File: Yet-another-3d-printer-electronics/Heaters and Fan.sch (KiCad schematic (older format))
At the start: 67 parts, among them P15 HEATER_BED, P16 HEATER_EXT, P18 FAN, P22 FAN, P23 HEATER_EXT, P4 FAN, Q1 2N7000, Q2 IRLR8743PBF, Q3 IRLML0030TRPBF, Q4 IRLR8743PBF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

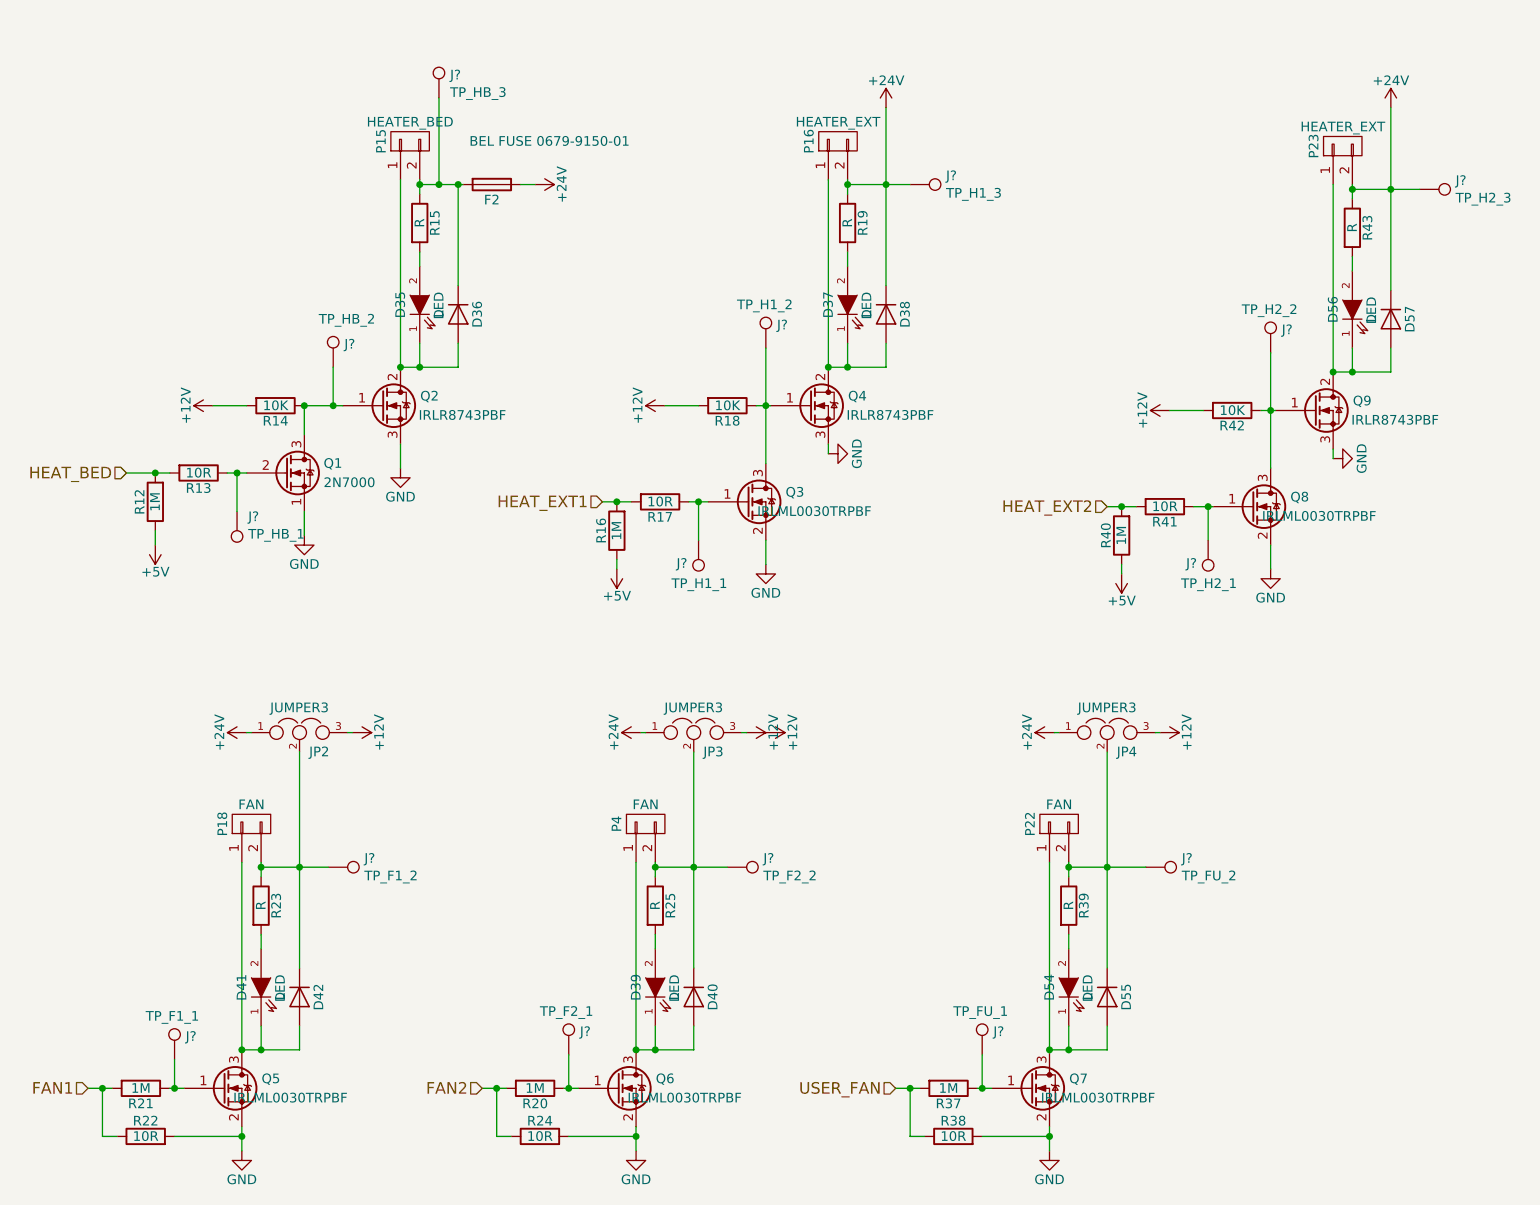
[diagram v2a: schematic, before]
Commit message: Choose footprints for TVS diode, heatbed, heaters, power socket and testpoints
Signed-off-by: Mateusz Krawczuk <mat.krawczuk@gmail.com>
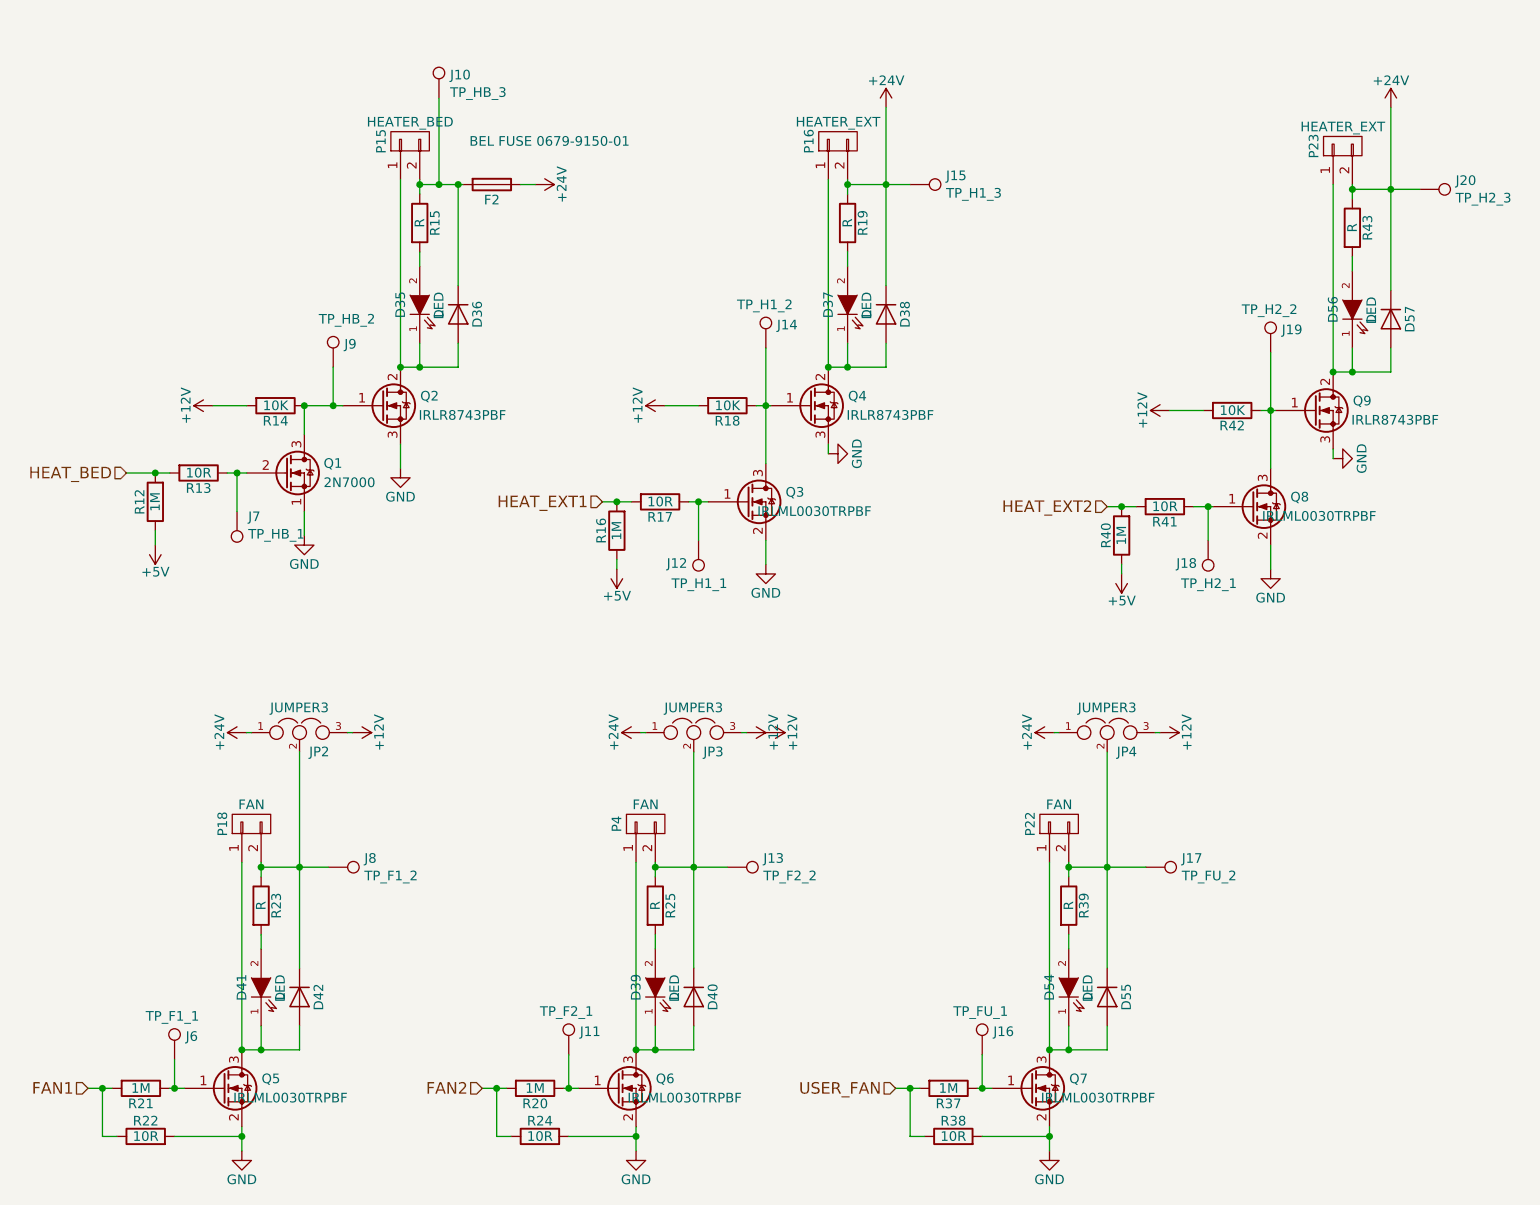
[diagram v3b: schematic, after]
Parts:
- J10, J11, J12, J13, J14, J15, J16, J17, J18, J19, J20, J6, J7, J8, J9: renamed from J?; footprint (none) -> Connect:PINTST
- JP2, JP3, JP4: footprint (none) -> Pin_Headers:Pin_Header_Straight_1x03_Pitch2.54mm
- P15: footprint Connectors:AK300-2 -> Yet-another-3d-printer-electronics:DG300-5.0-02P-12-00A(H)
- P16, P23: footprint Connectors:AK300-2 -> Yet-another-3d-printer-electronics:EBBA-02-C-SS-BU
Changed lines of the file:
@@
 F 0 "P15" H 2550 1775 50  0000 C CNN
 F 1 "HEATER_BED" V 2650 1625 50  0000 C CNN
-F 2 "Connectors:AK300-2" H 2550 1625 50  0001 C CNN
+F 2 "Yet-another-3d-printer-electronics:DG300-5.0-02P-12-00A(H)" H 2550 1625 50  0001 C CNN
 F 3 "" H 2550 1625 50  0000 C CNN
 	1    2550 1625
@@
 F 0 "P16" H 4775 1775 50  0000 C CNN
 F 1 "HEATER_EXT" V 4875 1625 50  0000 C CNN
-F 2 "Connectors:AK300-2" H 4775 1625 50  0001 C CNN
+F 2 "Yet-another-3d-printer-electronics:EBBA-02-C-SS-BU" H 4775 1625 50  0001 C CNN
 F 3 "" H 4775 1625 50  0000 C CNN
 	1    4775 1625
@@
 F 0 "JP2" H 2025 4600 50  0000 L CNN
 F 1 "JUMPER3" H 1975 4800 50  0000 C BNN
-F 2 "" H 1975 4700 50  0001 C CNN
+F 2 "Pin_Headers:Pin_Header_Straight_1x03_Pitch2.54mm" H 1975 4700 50  0001 C CNN
 F 3 "" H 1975 4700 50  0000 C CNN
 	1    1975 4700
@@
 F 0 "JP3" H 4075 4600 50  0000 L CNN
 F 1 "JUMPER3" H 4025 4800 50  0000 C BNN
-F 2 "" H 4025 4700 50  0001 C CNN
+F 2 "Pin_Headers:Pin_Header_Straight_1x03_Pitch2.54mm" H 4025 4700 50  0001 C CNN
 F 3 "" H 4025 4700 50  0000 C CNN
 	1    4025 4700
@@
 F 0 "JP4" H 6225 4600 50  0000 L CNN
 F 1 "JUMPER3" H 6175 4800 50  0000 C BNN
-F 2 "" H 6175 4700 50  0001 C CNN
+F 2 "Pin_Headers:Pin_Header_Straight_1x03_Pitch2.54mm" H 6175 4700 50  0001 C CNN
 F 3 "" H 6175 4700 50  0000 C CNN
 	1    6175 4700
@@
 F 0 "P23" H 7400 1800 50  0000 C CNN
 F 1 "HEATER_EXT" V 7500 1650 50  0000 C CNN
-F 2 "Connectors:AK300-2" H 7400 1650 50  0001 C CNN
+F 2 "Yet-another-3d-printer-electronics:EBBA-02-C-SS-BU" H 7400 1650 50  0001 C CNN
 F 3 "" H 7400 1650 50  0000 C CNN
 	1    7400 1650
@@
 $EndComp
 $Comp
-L TEST_1P J?
+L TEST_1P J10
 U 1 1 5985D991
 P 2700 1400
-F 0 "J?" H 2758 1520 50  0000 L CNN
+F 0 "J10" H 2758 1520 50  0000 L CNN
 F 1 "TP_HB_3" H 2758 1429 50  0000 L CNN
-F 2 "" H 2900 1400 50  0001 C CNN
+F 2 "Connect:PINTST" H 2900 1400 50  0001 C CNN
 F 3 "" H 2900 1400 50  0001 C CNN
 	1    2700 1400
@@
 $EndComp
 $Comp
-L TEST_1P J?
+L TEST_1P J15
 U 1 1 5985EA00
 P 5150 1850
-F 0 "J?" V 5104 2037 50  0000 L CNN
+F 0 "J15" V 5104 2037 50  0000 L CNN
 F 1 "TP_H1_3" V 5195 2037 50  0000 L CNN
-F 2 "" H 5350 1850 50  0001 C CNN
+F 2 "Connect:PINTST" H 5350 1850 50  0001 C CNN
 F 3 "" H 5350 1850 50  0001 C CNN
 	1    5150 1850
@@
 Connection ~ 2700 1850
 $Comp
-L TEST_1P J?
+L TEST_1P J20
 U 1 1 5985F8B9
 P 7800 1875
-F 0 "J?" V 7754 2062 50  0000 L CNN
+F 0 "J20" V 7754 2062 50  0000 L CNN
 F 1 "TP_H2_3" V 7845 2062 50  0000 L CNN
-F 2 "" H 8000 1875 50  0001 C CNN
+F 2 "Connect:PINTST" H 8000 1875 50  0001 C CNN
 F 3 "" H 8000 1875 50  0001 C CNN
 	1    7800 1875
@@
 $EndComp
 $Comp
-L TEST_1P J?
+L TEST_1P J8
 U 1 1 59860366
 P 2125 5400
-F 0 "J?" V 2079 5587 50  0000 L CNN
+F 0 "J8" V 2079 5587 50  0000 L CNN
 F 1 "TP_F1_2" V 2170 5587 50  0000 L CNN
-F 2 "" H 2325 5400 50  0001 C CNN
+F 2 "Connect:PINTST" H 2325 5400 50  0001 C CNN
 F 3 "" H 2325 5400 50  0001 C CNN
 	1    2125 5400
@@
 $EndComp
 $Comp
-L TEST_1P J?
+L TEST_1P J13
 U 1 1 598618D3
 P 4200 5400
-F 0 "J?" V 4154 5587 50  0000 L CNN
+F 0 "J13" V 4154 5587 50  0000 L CNN
 F 1 "TP_F2_2" V 4245 5587 50  0000 L CNN
-F 2 "" H 4400 5400 50  0001 C CNN
+F 2 "Connect:PINTST" H 4400 5400 50  0001 C CNN
 F 3 "" H 4400 5400 50  0001 C CNN
 	1    4200 5400
@@
 $EndComp
 $Comp
-L TEST_1P J?
+L TEST_1P J17
 U 1 1 59861B4C
 P 6375 5400
-F 0 "J?" V 6329 5588 50  0000 L CNN
+F 0 "J17" V 6329 5588 50  0000 L CNN
 F 1 "TP_FU_2" V 6420 5588 50  0000 L CNN
-F 2 "" H 6575 5400 50  0001 C CNN
+F 2 "Connect:PINTST" H 6575 5400 50  0001 C CNN
 F 3 "" H 6575 5400 50  0001 C CNN
 	1    6375 5400
@@
 $EndComp
 $Comp
-L TEST_1P J?
+L TEST_1P J9
 U 1 1 59864703
 P 2150 2800
-F 0 "J?" H 2208 2920 50  0000 L CNN
+F 0 "J9" H 2208 2920 50  0000 L CNN
 F 1 "TP_HB_2" H 2075 3050 50  0000 L CNN
-F 2 "" H 2350 2800 50  0001 C CNN
+F 2 "Connect:PINTST" H 2350 2800 50  0001 C CNN
 F 3 "" H 2350 2800 50  0001 C CNN
 	1    2150 2800
@@
 $EndComp
 $Comp
-L TEST_1P J?
+L TEST_1P J7
 U 1 1 59864CF5
 P 1650 3550
-F 0 "J?" H 1592 3577 50  0000 R CNN
+F 0 "J7" H 1592 3577 50  0000 R CNN
 F 1 "TP_HB_1" H 1592 3668 50  0000 R CNN
-F 2 "" H 1850 3550 50  0001 C CNN
+F 2 "Connect:PINTST" H 1850 3550 50  0001 C CNN
 F 3 "" H 1850 3550 50  0001 C CNN
 	1    1650 3550
@@
 Connection ~ 2150 3000
 $Comp
-L TEST_1P J?
+L TEST_1P J14
 U 1 1 59865BF7
 P 4400 2700
-F 0 "J?" H 4458 2820 50  0000 L CNN
+F 0 "J14" H 4458 2820 50  0000 L CNN
 F 1 "TP_H1_2" H 4250 2925 50  0000 L CNN
-F 2 "" H 4600 2700 50  0001 C CNN
+F 2 "Connect:PINTST" H 4600 2700 50  0001 C CNN
 F 3 "" H 4600 2700 50  0001 C CNN
 	1    4400 2700
@@
 $EndComp
 $Comp
-L TEST_1P J?
+L TEST_1P J12
 U 1 1 598667E9
 P 4050 3700
-F 0 "J?" H 4108 3820 50  0000 L CNN
+F 0 "J12" H 4108 3820 50  0000 L CNN
 F 1 "TP_H1_1" H 3900 3925 50  0000 L CNN
-F 2 "" H 4250 3700 50  0001 C CNN
+F 2 "Connect:PINTST" H 4250 3700 50  0001 C CNN
 F 3 "" H 4250 3700 50  0001 C CNN
 	1    4050 3700
@@
 Connection ~ 4050 3500
 $Comp
-L TEST_1P J?
+L TEST_1P J18
 U 1 1 5986795A
 P 6700 3700
-F 0 "J?" H 6758 3820 50  0000 L CNN
+F 0 "J18" H 6758 3820 50  0000 L CNN
 F 1 "TP_H2_1" H 6550 3925 50  0000 L CNN
-F 2 "" H 6900 3700 50  0001 C CNN
+F 2 "Connect:PINTST" H 6900 3700 50  0001 C CNN
 F 3 "" H 6900 3700 50  0001 C CNN
 	1    6700 3700
@@
 Connection ~ 6700 3525
 $Comp
-L TEST_1P J?
+L TEST_1P J19
 U 1 1 59867F55
 P 7025 2725
-F 0 "J?" H 7083 2845 50  0000 L CNN
+F 0 "J19" H 7083 2845 50  0000 L CNN
 F 1 "TP_H2_2" H 6875 2950 50  0000 L CNN
-F 2 "" H 7225 2725 50  0001 C CNN
+F 2 "Connect:PINTST" H 7225 2725 50  0001 C CNN
 F 3 "" H 7225 2725 50  0001 C CNN
 	1    7025 2725
@@
 $EndComp
 $Comp
-L TEST_1P J?
+L TEST_1P J6
 U 1 1 5986ACDE
 P 1325 6400
-F 0 "J?" H 1383 6520 50  0000 L CNN
+F 0 "J6" H 1383 6520 50  0000 L CNN
 F 1 "TP_F1_1" H 1175 6625 50  0000 L CNN
-F 2 "" H 1525 6400 50  0001 C CNN
+F 2 "Connect:PINTST" H 1525 6400 50  0001 C CNN
 F 3 "" H 1525 6400 50  0001 C CNN
 	1    1325 6400
@@
 $EndComp
 $Comp
-L TEST_1P J?
+L TEST_1P J11
 U 1 1 5986AE02
 P 3375 6375
-F 0 "J?" H 3433 6495 50  0000 L CNN
+F 0 "J11" H 3433 6495 50  0000 L CNN
 F 1 "TP_F2_1" H 3225 6600 50  0000 L CNN
-F 2 "" H 3575 6375 50  0001 C CNN
+F 2 "Connect:PINTST" H 3575 6375 50  0001 C CNN
 F 3 "" H 3575 6375 50  0001 C CNN
 	1    3375 6375
@@
 $EndComp
 $Comp
-L TEST_1P J?
+L TEST_1P J16
 U 1 1 5986AEDA
 P 5525 6375
-F 0 "J?" H 5583 6495 50  0000 L CNN
+F 0 "J16" H 5583 6495 50  0000 L CNN
 F 1 "TP_FU_1" H 5375 6600 50  0000 L CNN
-F 2 "" H 5725 6375 50  0001 C CNN
+F 2 "Connect:PINTST" H 5725 6375 50  0001 C CNN
 F 3 "" H 5725 6375 50  0001 C CNN
 	1    5525 6375

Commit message: Choose footprint for fuses and add TVS to power source connection
Signed-off-by: Mateusz Krawczuk <mat.krawczuk@gmail.com>
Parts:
- F2: footprint (none) -> Fuse_Holders_and_Fuses:Fuse_0679H
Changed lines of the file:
@@
 F 0 "F2" V 3055 1850 50  0000 C CNN
 F 1 "BEL FUSE 0679-9150-01" V 2750 2150 50  0000 C CNN
-F 2 "" V 2905 1850 50  0001 C CNN
+F 2 "Fuse_Holders_and_Fuses:Fuse_0679H" V 2905 1850 50  0001 C CNN
 F 3 "" H 2975 1850 50  0001 C CNN
 	1    2975 1850
